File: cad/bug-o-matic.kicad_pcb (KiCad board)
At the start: 4 copper layers, 83.8 x 31.8 mm, 71 parts, among them J1 USB_B, J10 VCCIO, J2 RS232, J4 VOUT, J5 AUX, J7 SWD/SERIAL, J8 CH_SWD, J9 JTAG, SW1 RESET, U1 MAX3232, U2 L78L33_TO92, U3 CH32V103C8T6, Y1 8M

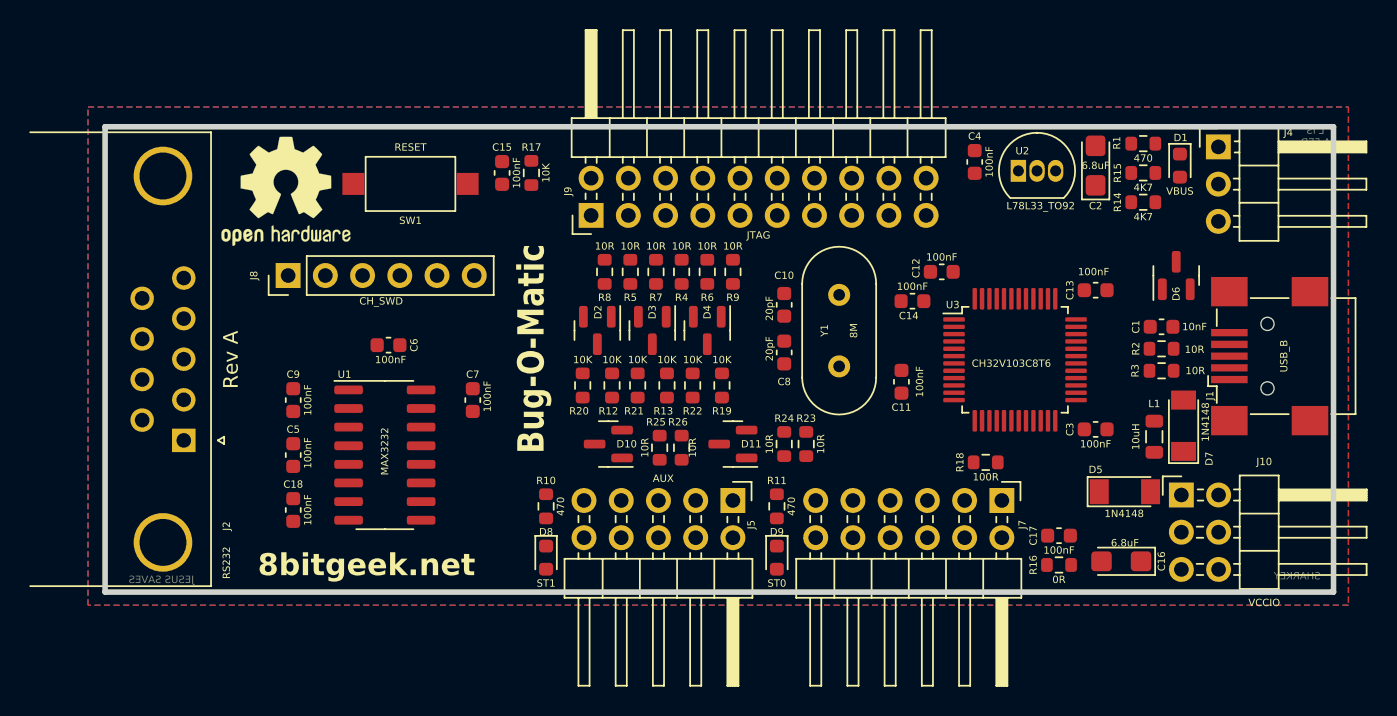
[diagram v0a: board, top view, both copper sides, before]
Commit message: 4 layer routing
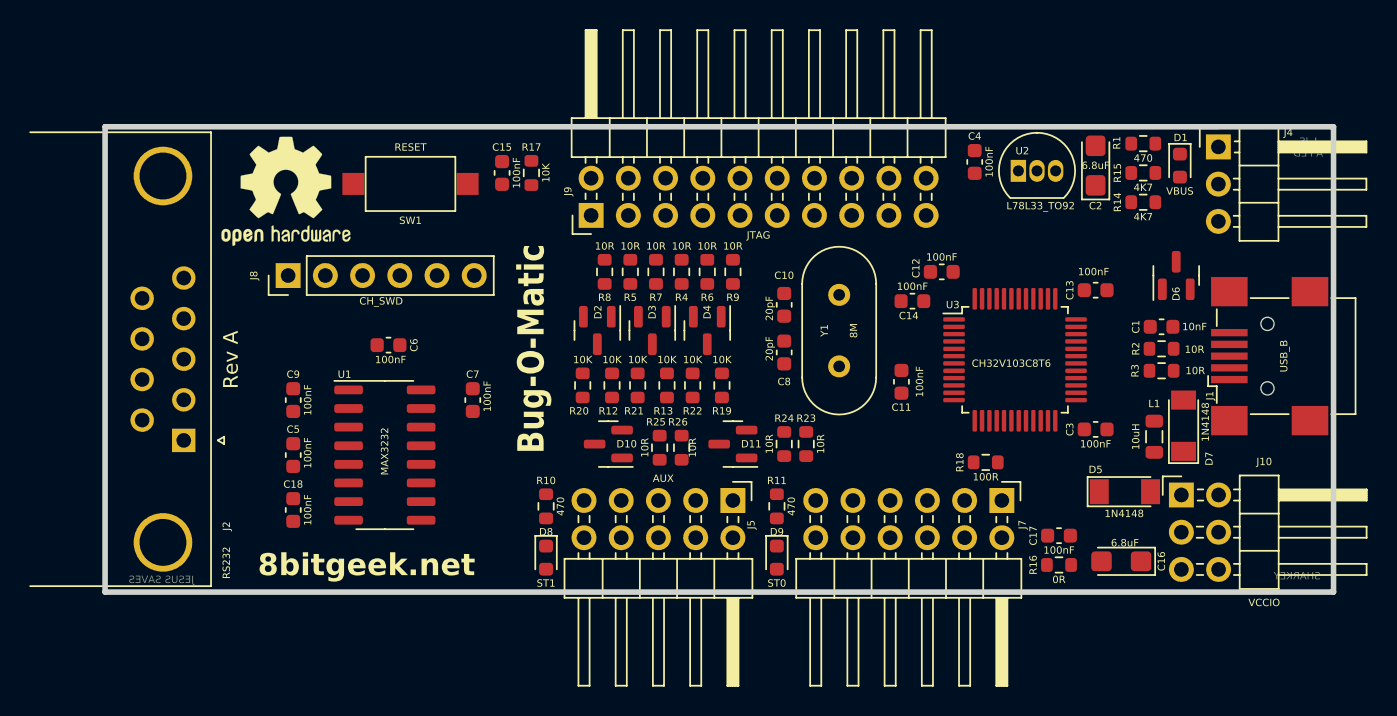
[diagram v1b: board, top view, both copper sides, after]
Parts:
- renumbered REF** to REF1, REF** to REF2
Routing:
- removed copper zone on B.Cu, net GND
- removed copper zone on F.Cu, net GND
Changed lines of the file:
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@@
 (kicad_pcb (version 20220427) (generator pcbnew)
   (general
-    (thickness 4.67)
+    (thickness 0)
   )
   (paper "A4")
   (layers
     (0 "F.Cu" mixed)
-    (1 "In1.Cu" power)
-    (2 "In2.Cu" power)
+    (1 "In1.Cu" mixed)
+    (2 "In2.Cu" mixed)
     (31 "B.Cu" mixed)
     (32 "B.Adhes" user "B.Adhesive")
@@
   )
   (setup
-    (stackup
-      (layer "F.Cu" (type "copper") (thickness 0.035))
-      (layer "dielectric 1" (type "core") (thickness 1.51) (material "FR4") (epsilon_r 4.5) (loss_tangent 0.02))
-      (layer "In1.Cu" (type "copper") (thickness 0.035))
-      (layer "dielectric 2" (type "prepreg") (thickness 1.51) (material "FR4") (epsilon_r 4.5) (loss_tangent 0.02))
-      (layer "In2.Cu" (type "copper") (thickness 0.035))
-      (layer "dielectric 3" (type "core") (thickness 1.51) (material "FR4") (epsilon_r 4.5) (loss_tangent 0.02))
-      (layer "B.Cu" (type "copper") (thickness 0.035))
-      (copper_finish "None")
-      (dielectric_constraints no)
-    )
     (pad_to_mask_clearance 0.051)
     (solder_mask_min_width 0.25)
@@
       (drillshape 0)
       (scaleselection 1)
-      (outputdirectory "cam/")
+      (outputdirectory "../cam/")
     )
   )
@@
     (fp_line (start 1.6 0.8) (end 1.6 -0.8)
       (stroke (width 0.1) (type solid)) (layer "F.Fab"))
-    (pad "1" smd roundrect (at -1.35 0 90) (size 1.4 1.35) (layers "F.Cu" "F.Paste" "F.Mask") (roundrect_rratio 0.185185)
+    (pad "1" smd roundrect (at -1.35 0 90) (size 1.4 1.35) (layers "F.Cu" "F.Paste" "F.Mask") (roundrect_rratio 0.1851851852)
       (net 3 "+5V") (pintype "passive"))
-    (pad "2" smd roundrect (at 1.35 0 90) (size 1.4 1.35) (layers "F.Cu" "F.Paste" "F.Mask") (roundrect_rratio 0.185185)
+    (pad "2" smd roundrect (at 1.35 0 90) (size 1.4 1.35) (layers "F.Cu" "F.Paste" "F.Mask") (roundrect_rratio 0.1851851852)
       (net 1 "GND") (pintype "passive"))
     (model "${KICAD6_3DMODEL_DIR}/Capacitor_Tantalum_SMD.3dshapes/CP_EIA-3216-18_Kemet-A.wrl"
@@
     (fp_line (start 1.6 0.8) (end 1.6 -0.8)
       (stroke (width 0.1) (type solid)) (layer "F.Fab"))
-    (pad "1" smd roundrect (at -1.35 0 180) (size 1.4 1.35) (layers "F.Cu" "F.Paste" "F.Mask") (roundrect_rratio 0.185185)
+    (pad "1" smd roundrect (at -1.35 0 180) (size 1.4 1.35) (layers "F.Cu" "F.Paste" "F.Mask") (roundrect_rratio 0.1851851852)
       (net 4 "+VSW") (pintype "passive"))
-    (pad "2" smd roundrect (at 1.35 0 180) (size 1.4 1.35) (layers "F.Cu" "F.Paste" "F.Mask") (roundrect_rratio 0.185185)
+    (pad "2" smd roundrect (at 1.35 0 180) (size 1.4 1.35) (layers "F.Cu" "F.Paste" "F.Mask") (roundrect_rratio 0.1851851852)
       (net 1 "GND") (pintype "passive"))
     (model "${KICAD6_3DMODEL_DIR}/Capacitor_Tantalum_SMD.3dshapes/CP_EIA-3216-18_Kemet-A.wrl"
@@
     (tags "Logo Symbol OSHW")
     (attr exclude_from_pos_files exclude_from_bom)
-    (fp_text reference "REF**" (at 0 0) (layer "F.SilkS") hide
+    (fp_text reference "REF1" (at 0 0) (layer "F.SilkS") hide
         (effects (font (size 1 1) (thickness 0.15)))
     )
@@
     (tags "Logo Symbol OSHW")
     (attr exclude_from_pos_files exclude_from_bom)
-    (fp_text reference "REF**" (at 0 0) (layer "B.SilkS") hide
+    (fp_text reference "REF2" (at 0 0) (layer "B.SilkS") hide
         (effects (font (size 1 1) (thickness 0.15)) (justify mirror))
     )
@@
     (effects (font (size 0.5 0.5) (thickness 0.125)) (justify mirror))
   )
-  (gr_text "L IS\nA FED" (at 201.75 67) (layer "B.Cu")
+  (gr_text "L IS\nA FED" (at 201.25 67.75) (layer "B.Cu")
     (effects (font (size 0.5 0.5) (thickness 0.125)) (justify mirror))
   )
@@
     (style (thickness 0.3048) (arrow_length 1.27) (text_position_mode 0) (extension_height 0.58642) (extension_offset 0) keep_text_aligned)
   )
-  (zone (net 1) (net_name "GND") (layer "F.Cu") (hatch edge 0.508)
-    (connect_pads (clearance 0.508))
-    (min_thickness 0.254) (filled_areas_thickness no)
-    (fill (thermal_gap 0.508) (thermal_bridge_width 0.508))
-    (polygon
-      (pts
-        (xy 204 99)
-        (xy 118 99)
-        (xy 118 65)
-        (xy 204 65)
-      )
-    )
-  )
-  (zone (net 1) (net_name "GND") (layer "B.Cu") (hatch edge 0.508)
-    (connect_pads (clearance 0.508))
-    (min_thickness 0.254) (filled_areas_thickness no)
-    (fill (thermal_gap 0.508) (thermal_bridge_width 0.508))
-    (polygon
-      (pts
-        (xy 204 99)
-        (xy 118 99)
-        (xy 118 65)
-        (xy 204 65)
-      )
-    )
-  )
 )

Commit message: preliminary artwork completed
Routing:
- net GND: track 0.00 -> 301.6 mm, vias 0 -> 17
- net +VSW: track 0.00 -> 135.3 mm, vias 0 -> 8
- net +5V: track 0.00 -> 70.7 mm, vias 0 -> 1
- net /VOUTR: track 0.00 -> 61.8 mm, vias 0 -> 2
- net /VTARGET: track 0.00 -> 61.2 mm
- net /AUX1: track 0.00 -> 52.6 mm, vias 0 -> 1
- net /CH_SWCLK: track 0.00 -> 51.6 mm, vias 0 -> 1
- net /CH_NRST: track 0.00 -> 50.8 mm, vias 0 -> 3
- net /CH_SWDIO: track 0.00 -> 47.8 mm, vias 0 -> 1
- net +3V3: track 0.00 -> 47.8 mm, vias 0 -> 2
- net /MCU-TDI: track 0.00 -> 42.5 mm, vias 0 -> 2
- net /ST0: track 0.00 -> 42.2 mm, vias 0 -> 2
- net /CH_SWO: track 0.00 -> 41.5 mm, vias 0 -> 1
- net /MCU_RS232_CTS: track 0.00 -> 40.3 mm, vias 0 -> 2
- net /MCU_RS232_RX: track 0.00 -> 40.1 mm, vias 0 -> 2
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- added copper zone on In2.Cu, net +VSW
- added copper zone on B.Cu, net GND
- added copper zone on F.Cu, net GND
- added copper zone on In1.Cu, net GND
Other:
- board text added: "Eat the bugs!"

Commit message: Revision A CAM generation
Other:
- board text added: "AUX0"
- board text added: "AUX1"
- board text added: "AUX2"
- board text added: "AUX3"
- board text added: "AUX4"
- board text added: "AUX5"
- board text added: "AUX6"
- board text added: "NRST"
- board text added: "SCL"
- board text added: "SDA"
- board text added: "SRST"
- board text added: "SWCLK"
- board text added: "SWDIO"
- board text added: "SWO"
- board text added: "TCK"
- board text added: "TDI"
- board text added: "TDO"
- board text added: "TMS"
- board text added: "TRST"
- board text added: "V+"
- board text added: "VIN"
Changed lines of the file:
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@@
     (effects (font (size 0.5 0.5) (thickness 0.125)) (justify mirror))
+  )
+  (gr_text "GND" (at 170 68.25) (layer "B.SilkS")
+    (effects (font (size 0.5 0.5) (thickness 0.125) bold) (justify mirror))
+  )
+  (gr_text "SRST" (at 170 74) (layer "B.SilkS")
+    (effects (font (size 0.5 0.5) (thickness 0.125) bold) (justify mirror))
+  )
+  (gr_text "GND" (at 172.75 68.25) (layer "B.SilkS")
+    (effects (font (size 0.5 0.5) (thickness 0.125) bold) (justify mirror))
+  )
+  (gr_text "+3V3" (at 162.25 90.25) (layer "B.SilkS")
+    (effects (font (size 0.5 0.5) (thickness 0.125) bold) (justify mirror))
+  )
+  (gr_text "VOUT" (at 152.25 68.25) (layer "B.SilkS")
+    (effects (font (size 0.5 0.5) (thickness 0.125) bold) (justify mirror))
+  )
+  (gr_text "NRST" (at 170.25 90.25) (layer "B.SilkS")
+    (effects (font (size 0.5 0.5) (thickness 0.125) bold) (justify mirror))
+  )
+  (gr_text "TRST" (at 154.75 74) (layer "B.SilkS")
+    (effects (font (size 0.5 0.5) (thickness 0.125) bold) (justify mirror))
+  )
+  (gr_text "GND" (at 162.5 68.25) (layer "B.SilkS")
+    (effects (font (size 0.5 0.5) (thickness 0.125) bold) (justify mirror))
+  )
+  (gr_text "TDO" (at 167.5 74) (layer "B.SilkS")
+    (effects (font (size 0.5 0.5) (thickness 0.125) bold) (justify mirror))
+  )
+  (gr_text "AUX3" (at 154.5 90.25) (layer "B.SilkS")
+    (effects (font (size 0.5 0.5) (thickness 0.125) bold) (justify mirror))
   )
   (gr_text "http://github.com/8bitgeek/bug-o-matic" (at 162.5 80.25) (layer "B.SilkS")
     (effects (font (size 1.5 1.5) (thickness 0.25) bold) (justify mirror))
   )
+  (gr_text "GND" (at 175.25 90.25) (layer "B.SilkS")
+    (effects (font (size 0.5 0.5) (thickness 0.125) bold) (justify mirror))
+  )
+  (gr_text "AUX2" (at 154.5 96.25) (layer "B.SilkS")
+    (effects (font (size 0.5 0.5) (thickness 0.125) bold) (justify mirror))
+  )
   (gr_text "VSWD" (at 197.75 94.25) (layer "B.SilkS")
     (effects (font (size 0.7 0.7) (thickness 0.175)) (justify mirror))
+  )
+  (gr_text "GND" (at 160 68.25) (layer "B.SilkS")
+    (effects (font (size 0.5 0.5) (thickness 0.125) bold) (justify mirror))
+  )
+  (gr_text "SDA" (at 170.25 96.25) (layer "B.SilkS")
+    (effects (font (size 0.5 0.5) (thickness 0.125) bold) (justify mirror))
+  )
+  (gr_text "GND" (at 157.5 68.25) (layer "B.SilkS")
+    (effects (font (size 0.5 0.5) (thickness 0.125) bold) (justify mirror))
+  )
+  (gr_text "GND" (at 175.25 96.25) (layer "B.SilkS")
+    (effects (font (size 0.5 0.5) (thickness 0.125) bold) (justify mirror))
+  )
+  (gr_text "TCK" (at 162.5 74) (layer "B.SilkS")
+    (effects (font (size 0.5 0.5) (thickness 0.125) bold) (justify mirror))
+  )
+  (gr_text "GND" (at 155 68.25) (layer "B.SilkS")
+    (effects (font (size 0.5 0.5) (thickness 0.125) bold) (justify mirror))
   )
   (gr_text "+VSW" (at 190 94.25) (layer "B.SilkS")
     (effects (font (size 0.7 0.7) (thickness 0.175)) (justify mirror))
   )
+  (gr_text "AUX1" (at 152 90.25) (layer "B.SilkS")
+    (effects (font (size 0.5 0.5) (thickness 0.125) bold) (justify mirror))
+  )
   (gr_text "VOUT" (at 190 91.75) (layer "B.SilkS")
     (effects (font (size 0.7 0.7) (thickness 0.175)) (justify mirror))
+  )
+  (gr_text "AUX0" (at 151.75 96.25) (layer "B.SilkS")
+    (effects (font (size 0.5 0.5) (thickness 0.125) bold) (justify mirror))
+  )
+  (gr_text "V+" (at 180.5 90.25) (layer "B.SilkS")
+    (effects (font (size 0.5 0.5) (thickness 0.125) bold) (justify mirror))
   )
   (gr_text "TXD" (at 125.8 84.9 90) (layer "B.SilkS")
@@
     (effects (font (size 0.7 0.7) (thickness 0.175)) (justify mirror))
   )
+  (gr_text "+5V" (at 162 96.25) (layer "B.SilkS")
+    (effects (font (size 0.5 0.5) (thickness 0.125) bold) (justify mirror))
+  )
+  (gr_text "TMS" (at 159.75 74) (layer "B.SilkS")
+    (effects (font (size 0.5 0.5) (thickness 0.125) bold) (justify mirror))
+  )
   (gr_text "VSENSE" (at 189.5 96.75) (layer "B.SilkS")
     (effects (font (size 0.7 0.7) (thickness 0.175)) (justify mirror))
@@
     (effects (font (size 0.508 0.508) (thickness 0.0762)) (justify mirror))
   )
+  (gr_text "SWCLK" (at 177.75 90.25) (layer "B.SilkS")
+    (effects (font (size 0.5 0.5) (thickness 0.125) bold) (justify mirror))
+  )
   (gr_text "CTS" (at 120.2 83.5 90) (layer "B.SilkS")
     (effects (font (size 0.508 0.508) (thickness 0.0762)) (justify mirror))
   )
+  (gr_text "SWDIO" (at 172.75 90.25) (layer "B.SilkS")
+    (effects (font (size 0.5 0.5) (thickness 0.125) bold) (justify mirror))
+  )
+  (gr_text "VSENSE" (at 198.5 96.75) (layer "B.SilkS")
+    (effects (font (size 0.7 0.7) (thickness 0.175)) (justify mirror))
+  )
+  (gr_text "AUX6" (at 159.5 96.25) (layer "B.SilkS")
+    (effects (font (size 0.5 0.5) (thickness 0.125) bold) (justify mirror))
+  )
   (gr_text "+5V" (at 192.75 72.75) (layer "B.SilkS")
     (effects (font (size 0.7 0.7) (thickness 0.175)) (justify mirror))
+  )
+  (gr_text "GND" (at 175.25 68.25) (layer "B.SilkS")
+    (effects (font (size 0.5 0.5) (thickness 0.125) bold) (justify mirror))
+  )
+  (gr_text "RXD" (at 177.75 96.25) (layer "B.SilkS")
+    (effects (font (size 0.5 0.5) (thickness 0.125) bold) (justify mirror))
+  )
+  (gr_text "TXD" (at 180.5 96.25) (layer "B.SilkS")
+    (effects (font (size 0.5 0.5) (thickness 0.125) bold) (justify mirror))
+  )
+  (gr_text "VOUT" (at 198.25 91.5) (layer "B.SilkS")
+    (effects (font (size 0.7 0.7) (thickness 0.175)) (justify mirror))
+  )
+  (gr_text "SCL" (at 172.75 96.25) (layer "B.SilkS")
+    (effects (font (size 0.5 0.5) (thickness 0.125) bold) (justify mirror))
+  )
+  (gr_text "AUX4" (at 157 96.25) (layer "B.SilkS")
+    (effects (font (size 0.5 0.5) (thickness 0.125) bold) (justify mirror))
+  )
+  (gr_text "VIN" (at 152.25 74) (layer "B.SilkS")
+    (effects (font (size 0.5 0.5) (thickness 0.125) bold) (justify mirror))
+  )
+  (gr_text "TDI" (at 157.25 74) (layer "B.SilkS")
+    (effects (font (size 0.5 0.5) (thickness 0.125) bold) (justify mirror))
+  )
+  (gr_text "SWO" (at 167.75 90.25) (layer "B.SilkS")
+    (effects (font (size 0.5 0.5) (thickness 0.125) bold) (justify mirror))
+  )
+  (gr_text "GND" (at 167.5 68.25) (layer "B.SilkS")
+    (effects (font (size 0.5 0.5) (thickness 0.125) bold) (justify mirror))
+  )
+  (gr_text "AUX5" (at 157 90.25) (layer "B.SilkS")
+    (effects (font (size 0.5 0.5) (thickness 0.125) bold) (justify mirror))
+  )
+  (gr_text "GND" (at 165 68.25) (layer "B.SilkS")
+    (effects (font (size 0.5 0.5) (thickness 0.125) bold) (justify mirror))
+  )
+  (gr_text "GND" (at 167.75 96.25) (layer "B.SilkS")
+    (effects (font (size 0.5 0.5) (thickness 0.125) bold) (justify mirror))
   )
   (gr_text "RXD" (at 125.9 82.2 90) (layer "B.SilkS")
@@
     (effects (font (size 0.508 0.508) (thickness 0.0762)) (justify mirror))
   )
+  (gr_text "GND" (at 159.5 90.25) (layer "B.SilkS")
+    (effects (font (size 0.5 0.5) (thickness 0.125) bold) (justify mirror))
+  )
   (gr_text "Rev A" (at 181.75 74) (layer "F.SilkS")
